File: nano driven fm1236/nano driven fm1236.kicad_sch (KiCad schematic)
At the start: 62 parts, among them J1 SPI, J2 address select, J3 Left, J4 Right, J5 SJ1-3525N, J6 AF, J7 2nd IF, J8 CVBS, SW1 Up, SW2 Down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

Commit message: made gerbers and added gitignore for kicad
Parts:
- added C19: 220uF, Capacitor_THT:C_Disc_D3.8mm_W2.6mm_P2.50mm, symbol Device:C_Polarized
- added J9: Barrel_Jack_Switch, Connector_BarrelJack:BarrelJack_Horizontal, symbol Connector:Barrel_Jack_Switch
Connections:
- net +5V: now also C19.1, J9.1
- net GND: now also C19.2, J9.2, J9.3
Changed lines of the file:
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@@
   (junction (at 79.375 128.27) (diameter 0) (color 0 0 0 0)
   )
+  (junction (at 104.14 33.02) (diameter 0) (color 0 0 0 0)
+  )
   (junction (at 166.37 73.025) (diameter 0) (color 0 0 0 0)
   )
@@
   )
   (junction (at 79.375 140.335) (diameter 0) (color 0 0 0 0)
+  )
+  (junction (at 109.22 25.4) (diameter 0) (color 0 0 0 0)
   )
   (junction (at 40.005 142.24) (diameter 0) (color 0 0 0 0)
@@
     (stroke (width 0) (type default) (color 0 0 0 0))
   )
+  (wire (pts (xy 109.22 27.94) (xy 109.22 25.4))
+    (stroke (width 0) (type default) (color 0 0 0 0))
+  )
   (wire (pts (xy 191.135 32.385) (xy 196.85 32.385))
     (stroke (width 0) (type default) (color 0 0 0 0))
   )
+  (wire (pts (xy 109.22 25.4) (xy 114.3 25.4))
+    (stroke (width 0) (type default) (color 0 0 0 0))
+  )
   (wire (pts (xy 160.02 160.655) (xy 165.1 160.655))
     (stroke (width 0) (type default) (color 0 0 0 0))
@@
     (stroke (width 0) (type default) (color 0 0 0 0))
   )
+  (wire (pts (xy 104.14 30.48) (xy 104.14 33.02))
+    (stroke (width 0) (type default) (color 0 0 0 0))
+  )
   (wire (pts (xy 168.91 113.03) (xy 168.91 105.41))
     (stroke (width 0) (type default) (color 0 0 0 0))
@@
     (stroke (width 0) (type default) (color 0 0 0 0))
   )
+  (wire (pts (xy 104.14 33.02) (xy 114.3 33.02))
+    (stroke (width 0) (type default) (color 0 0 0 0))
+  )
   (wire (pts (xy 79.375 128.27) (xy 64.77 128.27))
     (stroke (width 0) (type default) (color 0 0 0 0))
@@
   )
   (wire (pts (xy 138.43 168.275) (xy 150.495 168.275))
+    (stroke (width 0) (type default) (color 0 0 0 0))
+  )
+  (wire (pts (xy 104.14 27.94) (xy 109.22 27.94))
     (stroke (width 0) (type default) (color 0 0 0 0))
   )
@@
       (effects (font (size 1.27 1.27)) (justify left) hide)
     )
+  )
+  (symbol (lib_id "Connector:Barrel_Jack_Switch") (at 96.52 30.48 0) (unit 1)
+    (in_bom yes) (on_board yes) (fields_autoplaced)
+    (property "Reference" "J9" (id 0) (at 96.52 22.7035 0))
+    (property "Value" "Barrel_Jack_Switch" (id 1) (at 96.52 25.4786 0))
+    (property "Footprint" "Connector_BarrelJack:BarrelJack_Horizontal" (id 2) (at 97.79 31.496 0)
+      (effects (font (size 1.27 1.27)) hide)
+    )
+    (property "Datasheet" "~" (id 3) (at 97.79 31.496 0)
+      (effects (font (size 1.27 1.27)) hide)
+    )
+    (pin "1")
+    (pin "2")
+    (pin "3")
   )
   (symbol (lib_id "MCU_Module:Arduino_Nano_v3.x") (at 41.91 48.26 0) (mirror y) (unit 1)
@@
     (pin "2")
   )
+  (symbol (lib_id "power:+5V") (at 109.22 25.4 0) (unit 1)
+    (in_bom yes) (on_board yes) (fields_autoplaced)
+    (property "Reference" "#PWR0140" (id 0) (at 109.22 29.21 0)
+      (effects (font (size 1.27 1.27)) hide)
+    )
+    (property "Value" "+5V" (id 1) (at 109.22 21.7955 0))
+    (property "Footprint" "" (id 2) (at 109.22 25.4 0)
+      (effects (font (size 1.27 1.27)) hide)
+    )
+    (property "Datasheet" "" (id 3) (at 109.22 25.4 0)
+      (effects (font (size 1.27 1.27)) hide)
+    )
+    (pin "1")
+  )
   (symbol (lib_id "power:GND") (at 211.455 137.16 0) (unit 1)
     (in_bom yes) (on_board yes) (fields_autoplaced)
@@
     (pin "2")
     (pin "3")
+  )
+  (symbol (lib_id "power:GND") (at 104.14 33.02 0) (unit 1)
+    (in_bom yes) (on_board yes) (fields_autoplaced)
+    (property "Reference" "#PWR0139" (id 0) (at 104.14 39.37 0)
+      (effects (font (size 1.27 1.27)) hide)
+    )
+    (property "Value" "GND" (id 1) (at 104.14 37.5825 0))
+    (property "Footprint" "" (id 2) (at 104.14 33.02 0)
+      (effects (font (size 1.27 1.27)) hide)
+    )
+    (property "Datasheet" "" (id 3) (at 104.14 33.02 0)
+      (effects (font (size 1.27 1.27)) hide)
+    )
+    (pin "1")
   )
   (symbol (lib_id "Device:C") (at 259.715 46.355 90) (unit 1)
@@
     (pin "2")
   )
+  (symbol (lib_id "Device:C_Polarized") (at 114.3 29.21 0) (unit 1)
+    (in_bom yes) (on_board yes) (fields_autoplaced)
+    (property "Reference" "C19" (id 0) (at 117.221 27.4125 0)
+      (effects (font (size 1.27 1.27)) (justify left))
+    )
+    (property "Value" "220uF" (id 1) (at 117.221 30.1876 0)
+      (effects (font (size 1.27 1.27)) (justify left))
+    )
+    (property "Footprint" "Capacitor_THT:C_Disc_D3.8mm_W2.6mm_P2.50mm" (id 2) (at 115.2652 33.02 0)
+      (effects (font (size 1.27 1.27)) hide)
+    )
+    (property "Datasheet" "~" (id 3) (at 114.3 29.21 0)
+      (effects (font (size 1.27 1.27)) hide)
+    )
+    (pin "1")
+    (pin "2")
+  )
   (symbol (lib_id "power:+5V") (at 161.925 24.765 0) (unit 1)
     (in_bom yes) (on_board yes) (fields_autoplaced)
@@
       (reference "#PWR0138") (unit 1) (value "GND") (footprint "")
     )
+    (path "/98f19deb-c1d4-4e23-9fcb-5c4c17204212"
+      (reference "#PWR0139") (unit 1) (value "GND") (footprint "")
+    )
+    (path "/3d6a71ff-cf04-4b4e-90fb-9eea8990a7a5"
+      (reference "#PWR0140") (unit 1) (value "+5V") (footprint "")
+    )
     (path "/02663bc3-3260-4a72-85af-c0d3b4b277cb"
       (reference "A1") (unit 1) (value "Arduino_Nano_v3.x") (footprint "Module:Arduino_Nano")
@@
       (reference "C18") (unit 1) (value "10nF") (footprint "Capacitor_SMD:C_0603_1608Metric")
     )
+    (path "/fbca894a-649f-401e-a7f0-3653d82cdd60"
+      (reference "C19") (unit 1) (value "220uF") (footprint "Capacitor_THT:C_Disc_D3.8mm_W2.6mm_P2.50mm")
+    )
     (path "/0beb7083-4da5-4dbb-af4f-e5bc1f6cf1be"
       (reference "D1") (unit 1) (value "Radio") (footprint "LED_THT:LED_D3.0mm")
@@
       (reference "J8") (unit 1) (value "CVBS") (footprint "Evan's misc parts:CUI_RCJ-013")
     )
+    (path "/01acb040-f423-491c-bd6f-dbe3cfa66fbb"
+      (reference "J9") (unit 1) (value "Barrel_Jack_Switch") (footprint "Connector_BarrelJack:BarrelJack_Horizontal")
+    )
     (path "/7fdcf920-1b9e-45d2-a2ad-cb4d0eb7f444"

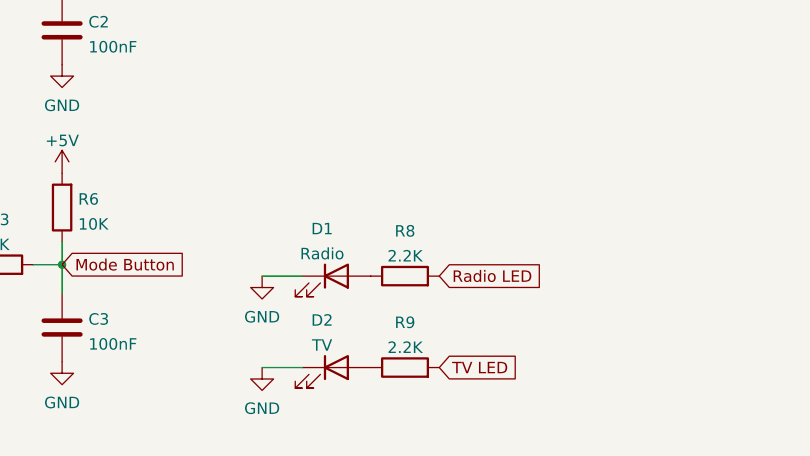
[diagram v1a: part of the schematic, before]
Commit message: added datasheet(s) notes and example for running the 7-segments
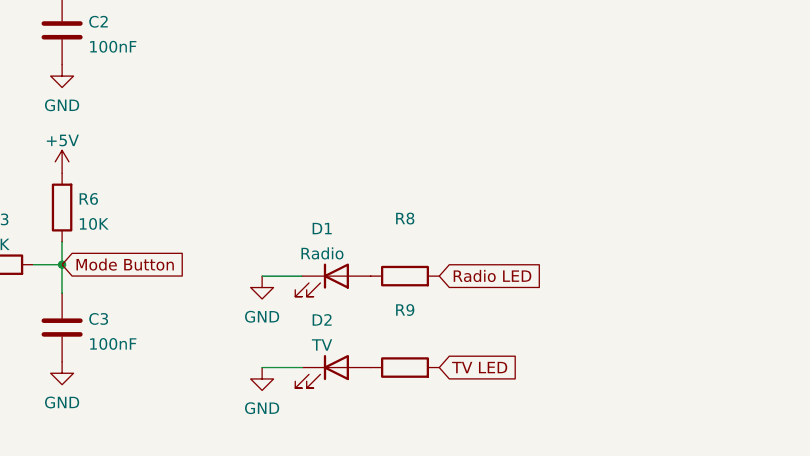
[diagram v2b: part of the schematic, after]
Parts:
- R8, R9: value 2.2K -> (none)
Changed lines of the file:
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@@
   (symbol (lib_id "Device:R") (at 78.105 186.69 90) (unit 1)
     (in_bom yes) (on_board yes) (fields_autoplaced)
-    (property "Reference" "R9" (id 0) (at 78.105 181.7075 90))
-    (property "Value" "2.2K" (id 1) (at 78.105 184.4826 90))
+    (property "Reference" "R9" (id 0) (at 78.105 180.34 90))
+    (property "Value" "" (id 1) (at 78.105 182.88 90))
     (property "Footprint" "Resistor_SMD:R_0603_1608Metric" (id 2) (at 78.105 188.468 90)
       (effects (font (size 1.27 1.27)) hide)
@@
     (pin "2")
     (pin "3")
+    (pin "5")
+    (pin "6")
+    (pin "7")
+    (pin "4")
+    (pin "8")
   )
   (symbol (lib_id "power:GND") (at 104.14 33.02 0) (unit 1)
@@
       (effects (font (size 1.27 1.27)) hide)
     )
+    (pin "1")
+    (pin "2")
+    (pin "3")
     (pin "5")
     (pin "6")
     (pin "7")
+    (pin "4")
+    (pin "8")
   )
   (symbol (lib_id "Device:C") (at 250.825 24.13 0) (unit 1)
@@
       (effects (font (size 1.27 1.27)) hide)
     )
+    (pin "1")
+    (pin "2")
+    (pin "3")
+    (pin "5")
+    (pin "6")
+    (pin "7")
     (pin "4")
     (pin "8")
@@
   (symbol (lib_id "Device:R") (at 78.105 176.53 90) (unit 1)
     (in_bom yes) (on_board yes) (fields_autoplaced)
-    (property "Reference" "R8" (id 0) (at 78.105 171.5475 90))
-    (property "Value" "2.2K" (id 1) (at 78.105 174.3226 90))
+    (property "Reference" "R8" (id 0) (at 78.105 170.18 90))
+    (property "Value" "" (id 1) (at 78.105 172.72 90))
     (property "Footprint" "Resistor_SMD:R_0603_1608Metric" (id 2) (at 78.105 178.308 90)
       (effects (font (size 1.27 1.27)) hide)
@@
     )
     (path "/f6ef7aa5-8305-4033-8e6f-bb8c08f794bf"
-      (reference "R8") (unit 1) (value "2.2K") (footprint "Resistor_SMD:R_0603_1608Metric")
+      (reference "R8") (unit 1) (value "1K") (footprint "Resistor_SMD:R_0603_1608Metric")
     )
     (path "/756d829d-a819-4d17-875b-8bb3165d33e2"
-      (reference "R9") (unit 1) (value "2.2K") (footprint "Resistor_SMD:R_0603_1608Metric")
+      (reference "R9") (unit 1) (value "1K") (footprint "Resistor_SMD:R_0603_1608Metric")
     )
     (path "/4ca624b9-a7a1-4842-bc72-df5ffd5938ba"
